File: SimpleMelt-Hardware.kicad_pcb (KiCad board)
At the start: 2 copper layers, 61.9 x 21.5 mm, 108 parts, among them J1 Conn_01x02, J2 Conn_01x02, J200 SH_PPM, J201 SH_LED, J202 SH_LED, J60 Conn_Coaxial, Q20 AO3401A, Q30 LBSS84LT1G, Q31 2N7002, Q32 LBSS84LT1G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

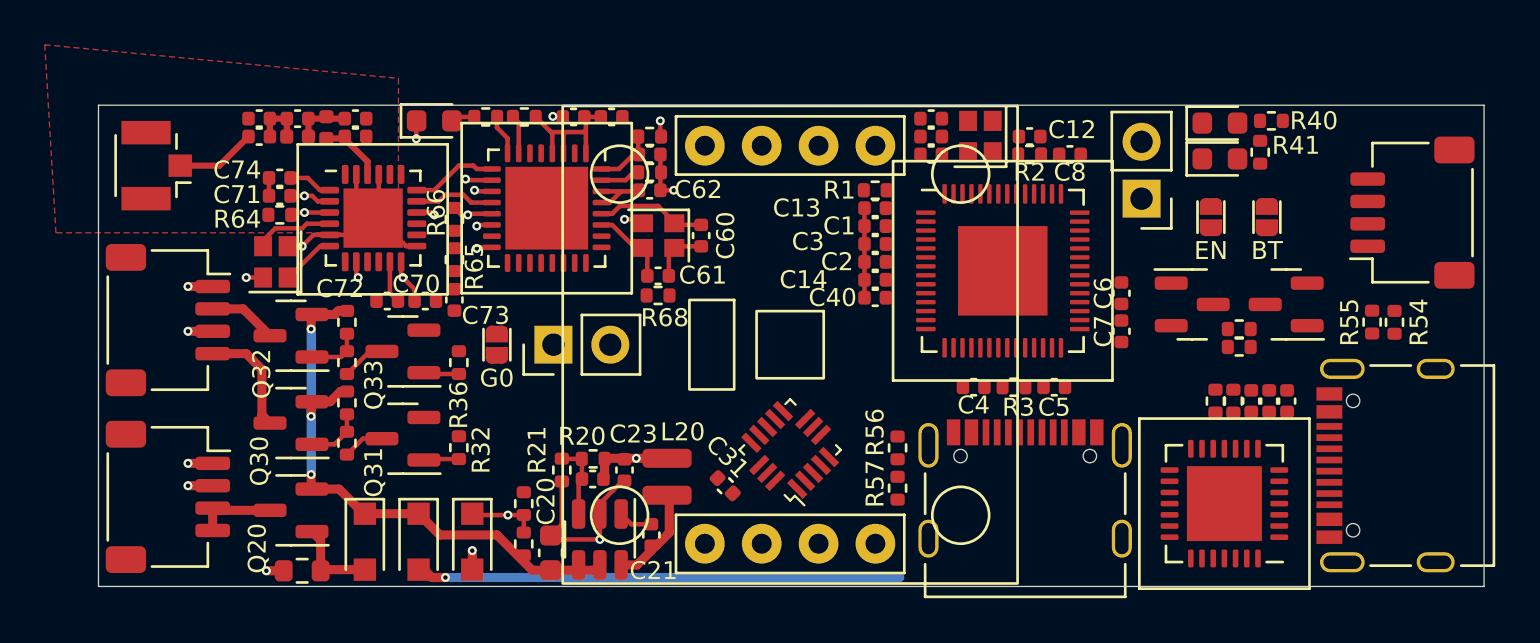
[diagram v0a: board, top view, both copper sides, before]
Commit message: All traces routed for V1
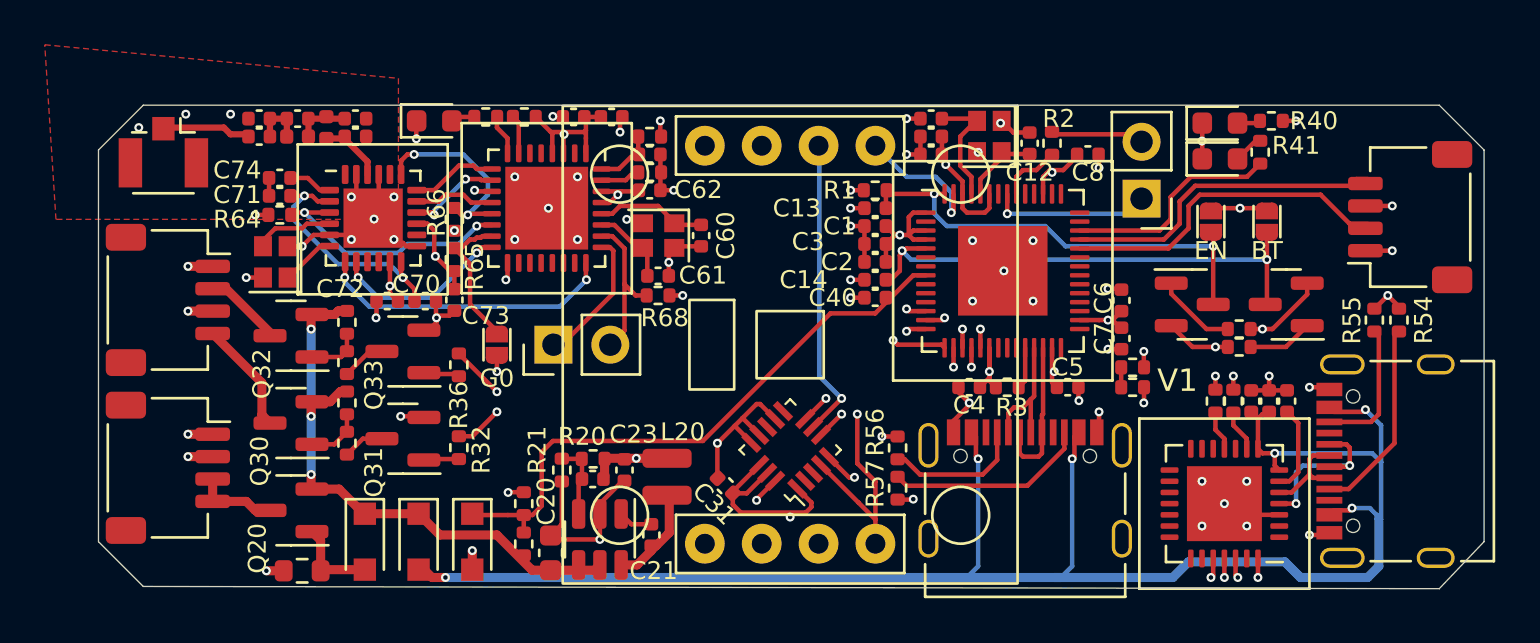
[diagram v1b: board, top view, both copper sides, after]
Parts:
- added G***: LOGO, AlfredoFootprints:Alfredo_logo_small, B.Cu at (-25.9, -5.80)
- added R4: 7K, Resistor_SMD:R_0402_1005Metric, F.Cu at (15.3, 1.90)
- added R5: 1K, Resistor_SMD:R_0402_1005Metric, F.Cu at (15.3, 1.01)
- moved J202 1.30 mm to (-27.8, 5.50)
- moved R2 1.12 mm to (11.7, -9.00), turned to -90 degrees
- moved J201 0.90 mm to (-27.8, -2.00)
- moved C8 0.80 mm to (13.3, -8.50)
- moved J60 0.67 mm to (-28.0, -8.60), turned to -90 degrees
- moved C5 0.60 mm to (12.4, 1.90), turned to 180 degrees
- moved U2 0.40 mm to (8.90, -9.30)
- moved C7 0.32 mm to (14.8, -0.28)
- moved C6 0.32 mm to (14.8, -1.98), turned to -90 degrees
- moved C12 0.30 mm to (10.7, -9.00), turned to -90 degrees
- moved R3 0.30 mm to (9.70, 1.90)
- moved J200 0.22 mm to (27.7, -5.70)
- moved R54 0.22 mm to (27.2, -1.10)
- moved JP1 0.20 mm to (21.3, -5.50)
- moved JP2 0.20 mm to (18.8, -5.50)
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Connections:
- J200 pad 2: PPM_B -> PPM_F
- J200 pad 4: PPM_F -> PPM_B
- U1 pad 12: unconnected-(U1-Pad12) -> X_TX
- U1 pad 13: unconnected-(U1-Pad13) -> X_RX
- U1 pad 14: unconnected-(U1-Pad14) -> LED_2
- U1 pad 15: unconnected-(U1-Pad15) -> LED_1
- U1 pad 16: unconnected-(U1-Pad16) -> P_SCK
- U1 pad 17: unconnected-(U1-Pad17) -> A1_CS
- U1 pad 18: unconnected-(U1-Pad18) -> P_MOSI
- U1 pad 19: unconnected-(U1-Pad19) -> P_MISO
- U1 pad 38: unconnected-(U1-Pad38) -> PPM_F
- U1 pad 39: unconnected-(U1-Pad39) -> PPM_B
- U1 pad 40: unconnected-(U1-Pad40) -> LED_MISC
- U1 pad 55: unconnected-(U1-Pad55) -> A2_CS
- U1 pad 8: unconnected-(U1-Pad8) -> SNS_VIN
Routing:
- net VBUS: track 21.6 -> 78.5 mm, vias 1 -> 6
- net GND: track 37.6 -> 80.6 mm, vias 13 -> 73
- net +3V3: track 16.8 -> 56.9 mm, vias 3 -> 21
- net E_RXD: track 0.00 -> 27.5 mm, vias 0 -> 2
- net E_TXD: track 0.00 -> 27.4 mm, vias 0 -> 1
- net X_RX: track 0.00 -> 26.0 mm, vias 0 -> 1
- net SNS_VIN: track 3.10 -> 27.0 mm, vias 1 -> 0
- net LED_1: track 0.00 -> 23.7 mm, vias 0 -> 2
- net LED_2: track 0.00 -> 22.8 mm, vias 0 -> 2
- net E_IO0: track 0.00 -> 22.6 mm, vias 0 -> 2
- net P_MISO: track 0.00 -> 21.8 mm, vias 0 -> 2
- net X_TX: track 0.00 -> 21.8 mm, vias 0 -> 1
- net E_EN: track 0.00 -> 20.6 mm, vias 0 -> 2
- net CP_RTS: track 0.00 -> 16.8 mm, vias 0 -> 2
- net CP_DTR: track 0.00 -> 16.3 mm, vias 0 -> 2
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- added copper zone on In2.Cu, net +3V3
- added copper zone on In1.Cu, net GND
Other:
- board size 61.9 x 21.5 mm -> 61.9 x 21.6 mm
- copper layers 2 -> 4
- board text added: "SimpleMelt V1"
- board text added: "V1"
- board text added: "© 2022 Alfredo Systems"

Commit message: All LCSC components selected
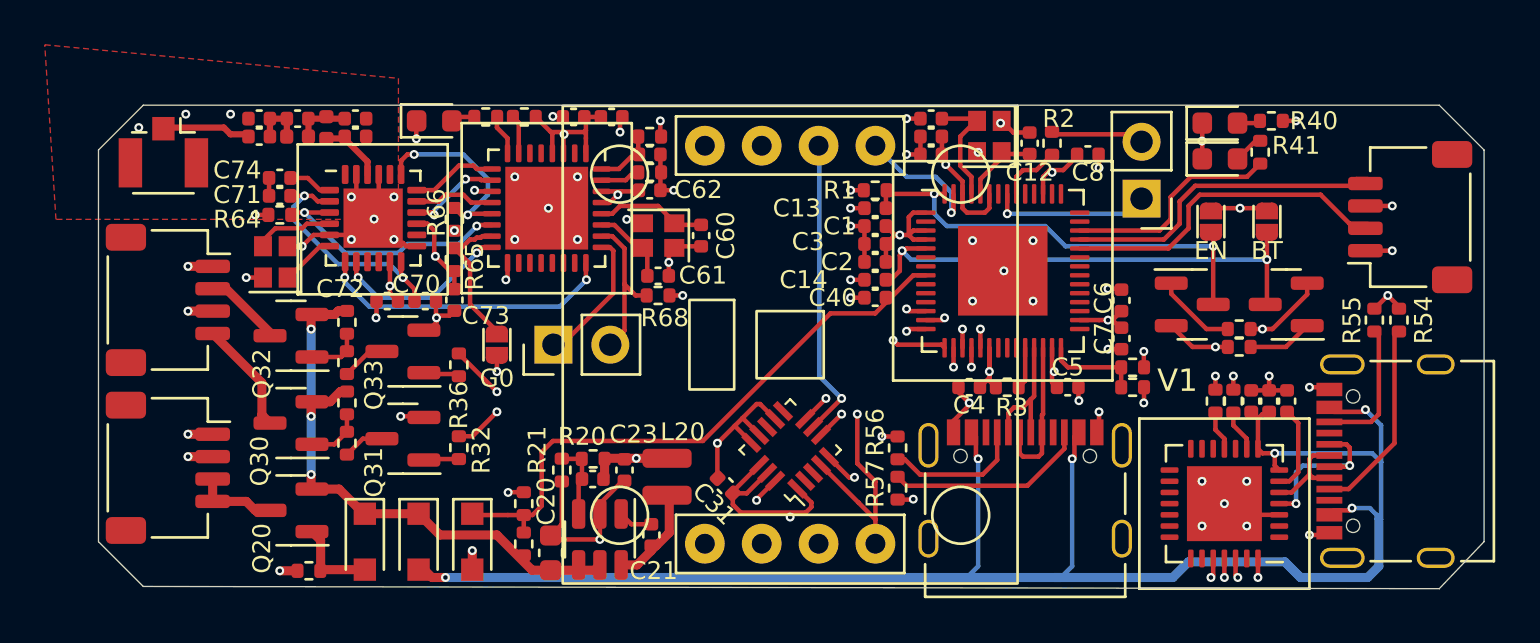
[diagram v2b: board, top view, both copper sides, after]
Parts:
- R22: footprint Resistor_SMD:R_0603_1608Metric -> Resistor_SMD:R_0402_1005Metric
- moved R22 0.30 mm to (-21.5, 10.1)
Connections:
- U1 pad 28: unconnected-(U1-Pad28) -> Net-(R4-Pad1)
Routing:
- net Net-(R4-Pad1): track 0.79 -> 4.17 mm

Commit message: Rotini V1
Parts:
- added R10: 300R, Resistor_SMD:R_1206_3216Metric, F.Cu at (-4.80, 2.00)
- added R6: 300R, Resistor_SMD:R_1206_3216Metric, F.Cu at (-0.99, -2.20)
- added R7: 300R, Resistor_SMD:R_1206_3216Metric, F.Cu at (-1.00, -6.40)
- added R8: 300R, Resistor_SMD:R_1206_3216Metric, F.Cu at (-1.00, -4.30)
- added R9: 300R, Resistor_SMD:R_1206_3216Metric, F.Cu at (-2.80, -0.10)
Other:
- board text added: "Rotini V1"
- board text removed: "SimpleMelt V1"
